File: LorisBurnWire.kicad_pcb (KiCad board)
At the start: 2 copper layers, 63 parts, among them J1 BurnWire, J2 BurnWire, J3 BurnWire, J4 BurnWire, Q1 BUK7M6R3-40EX, Q2 BUK7M6R3-40EX, Q3 BUK7M6R3-40EX, Q4 BUK7M6R3-40EX, U1 TLC555ID, U2 TLC555ID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

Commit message: Rough layout of PCB
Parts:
- moved R11 111.3 mm to (88.5, 133.3), turned to 180 degrees
- moved D1 110.8 mm to (151.1, 126.4), turned to 270 degrees
- moved R19 108.4 mm to (80.0, 134.6), turned to 270 degrees
- moved C1 107.5 mm to (151.5, 122.6)
- moved C17 106.4 mm to (152.4, 80.6), turned to 180 degrees
- moved C19 103.8 mm to (161.3, 79.4), turned to 270 degrees
- moved R2 103.3 mm to (121.1, 133.3), turned to 180 degrees
- moved D3 102.0 mm to (181.6, 127.0), turned to 270 degrees
- moved R20 100.4 mm to (74.9, 133.3), turned to 180 degrees
- moved C3 100.1 mm to (151.1, 133.3)
- moved R6 100.1 mm to (104.1, 133.3), turned to 180 degrees
- moved Q1 99.0 mm to (123.2, 128.3), turned to 90 degrees
- moved R9 98.7 mm to (93.3, 134.6), turned to 270 degrees
- moved D2 98.6 mm to (167.0, 127.0), turned to 270 degrees
- moved R1 98.2 mm to (126.4, 134.6), turned to 270 degrees
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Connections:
- J1 pad 1: Net-(J1-Pad1) -> PWR_FLAG
- J2 pad 1: Net-(J1-Pad1) -> PWR_FLAG
- J3 pad 1: Net-(J1-Pad1) -> PWR_FLAG
- J4 pad 1: Net-(J1-Pad1) -> PWR_FLAG
- R15 pad 1: Net-(R15-Pad1) -> PWR_FLAG
- R18 pad 1: Net-(R15-Pad1) -> PWR_FLAG
- U5 pad 4: Net-(R15-Pad1) -> PWR_FLAG
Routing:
- net +5V: track 0.00 -> 247.1 mm
- net GND: track 0.00 -> 185.4 mm, vias 0 -> 15
- net PWR_FLAG: track 0.00 -> 132.2 mm
- net /WireCutter4: track 0.00 -> 127.7 mm
- net /WireCutter3: track 0.00 -> 100.0 mm
- net PACK+: track 0.00 -> 76.3 mm
- net /WireCutter2: track 0.00 -> 68.7 mm
- net /WireCutter1: track 0.00 -> 39.0 mm
- net Net-(C8-Pad2): track 0.00 -> 32.2 mm
- net Net-(R12-Pad1): track 0.00 -> 19.8 mm
- net Net-(C3-Pad2): track 0.00 -> 19.8 mm
- net Net-(C6-Pad2): track 0.00 -> 17.5 mm
- net Net-(C10-Pad2): track 0.00 -> 17.1 mm
- net Net-(J1-Pad2): track 0.00 -> 12.4 mm
- net Net-(J4-Pad2): track 0.00 -> 12.3 mm
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- added copper zone on B.Cu, net GND
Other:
- board text added: "+5V"
- board text added: "PWR_FLAG"
- board text added: "Pack+"
- board text added: "WireCutter1"
- board text added: "WireCutter2"
- board text added: "WireCutter3"
- board text added: "WireCutter4"

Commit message: edits
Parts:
- added J5: TimerTestPoints, Connector_PinHeader_2.54mm:PinHeader_1x04_P2.54mm_Vertical, F.Cu at (141.5, 126.7)
- added J6: PACK+, TempoFootprints:TE_282837-2, F.Cu at (124.5, 70.4)
- added J7: TestPointCurrentLimiter, Connector_PinHeader_2.54mm:PinHeader_1x02_P2.54mm_Vertical, F.Cu at (133.9, 93.7)
- moved J3 102.3 mm to (186.2, 84.1), turned to 90 degrees
- moved Q4 99.2 mm to (135.1, 47.5)
- moved J4 97.6 mm to (135.6, 39.1), turned to 180 degrees
- moved Q3 97.5 mm to (178.3, 84.1), turned to 0 degrees
- moved R20 88.4 mm to (162.6, 121.9), turned to 0 degrees
- moved R19 78.7 mm to (157.5, 120.7), turned to 90 degrees
- moved R11 60.5 mm to (148.0, 122.2), turned to 0 degrees
- moved R9 51.6 mm to (143.1, 120.9), turned to 90 degrees
- moved Q1 50.7 mm to (94.0, 86.9), turned to 0 degrees
- moved J1 48.2 mm to (83.6, 87.9), turned to 270 degrees
- moved J2 41.4 mm to (136.0, 142.7)
- moved C10 38.4 mm to (146.2, 115.2)
- moved C1 38.4 mm to (118.0, 103.8)
- moved C7 38.4 mm to (147.9, 103.1)
- moved D3 38.4 mm to (148.1, 108.2)
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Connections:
- net /WireCutter1 renamed WireCutter1
- net /WireCutter2 renamed WireCutter2
- net /WireCutter3 renamed WireCutter3
- net /WireCutter4 renamed WireCutter4
- net Net-(C8-Pad2) renamed OUT
- net PWR_FLAG renamed VS
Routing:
- net +5V: track 247.1 -> 7.26 mm
- net GND: track 185.4 -> 38.2 mm, vias 15 -> 50
- net WireCutter4: track 127.7 -> 22.1 mm, vias 0 -> 1
- net VS: track 132.2 -> 235.4 mm, vias 0 -> 2
- net Net-(Q4-Pad4): track 8.48 -> 90.4 mm
- net WireCutter3: track 100.0 -> 22.6 mm, vias 0 -> 1
- net Net-(Q3-Pad4): track 8.44 -> 66.1 mm
- net Net-(Q1-Pad4): track 8.11 -> 60.7 mm
- net WireCutter2: track 68.7 -> 31.0 mm
- net PACK+: track 76.3 -> 57.1 mm
- net Net-(Q2-Pad4): track 8.75 -> 15.7 mm, vias 0 -> 1
- net OUT: track 32.2 -> 38.0 mm
- net WireCutter1: track 39.0 -> 43.8 mm
- net Net-(J3-Pad2): track 12.3 -> 8.52 mm
- net Net-(J4-Pad2): track 12.3 -> 8.82 mm
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- added copper zone on F.Cu, net +5V
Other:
- net class Vs added: clearance 0.2, trace_width 2, via_dia 0.8, via_drill 0.4
- net class high current added: clearance 0.2, trace_width 0.75, via_dia 0.8, via_drill 0.4
- board text removed: "Pack+"

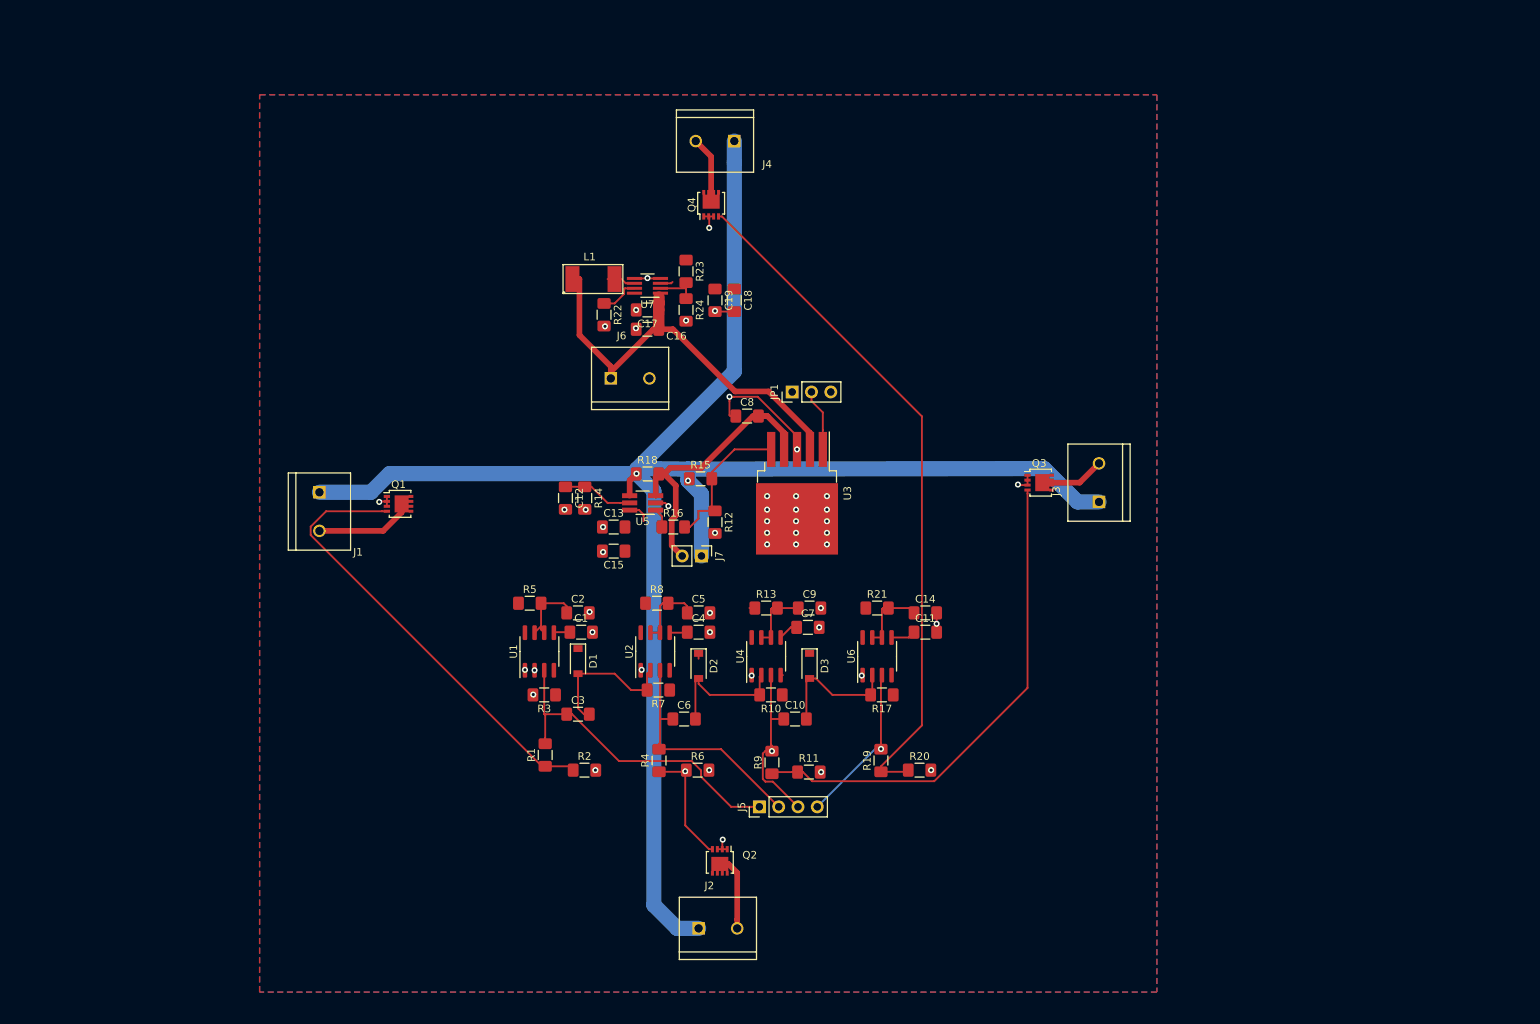
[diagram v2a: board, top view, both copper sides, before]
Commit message: changed trace width
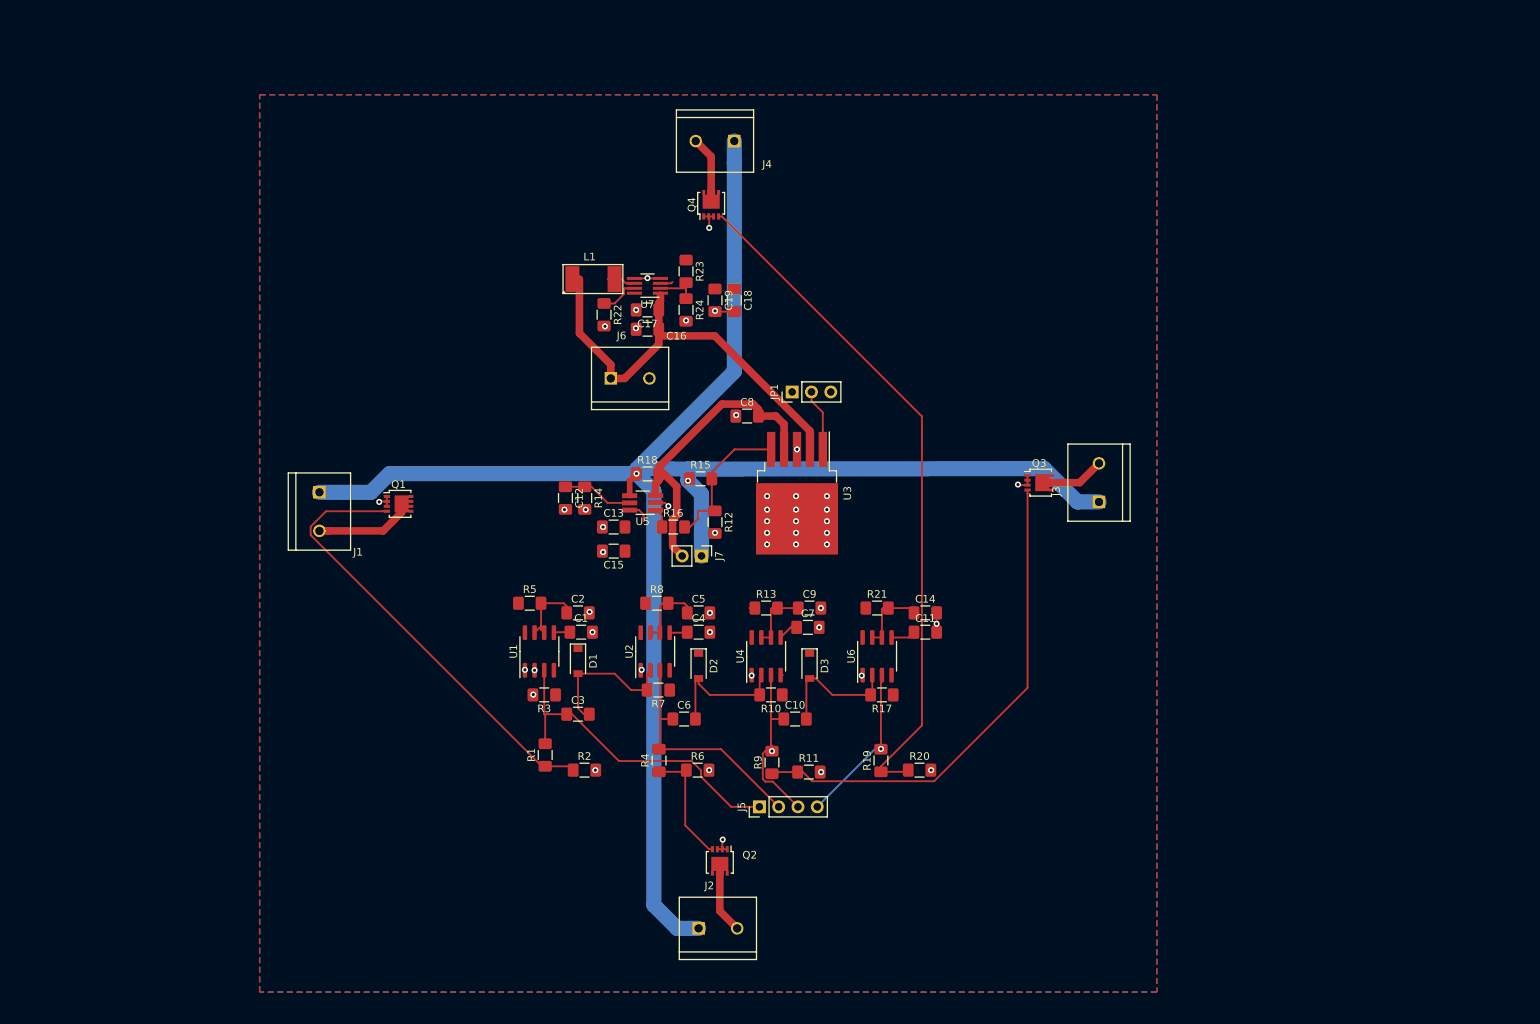
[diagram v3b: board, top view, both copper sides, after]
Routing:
- net GND: track 38.2 -> 23.8 mm
- net OUT: track 38.0 -> 41.6 mm
- net +5V: track 7.26 -> 6.56 mm
- net Net-(J2-Pad2): track 10.1 -> 9.43 mm
- net Net-(Q2-Pad4): vias 1 -> 0
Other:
- net class high current: trace_width 0.75 -> 1
- board text removed: "+5V"
